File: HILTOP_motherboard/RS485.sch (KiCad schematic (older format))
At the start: 42 parts, among them U13 AM1S-0505SZ, U15 ISO3080, U16 ISO3080, U17 AM1S-0505SZ, U18 USB6B1, U19 USB6B1, U20 USB6B1, U21 USB6B1, U43 MAX3107, U44 MAX3107, Y8 3.6864MHz Crystal, Y9 3.6864MHz Crystal

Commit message: nearly finished placing all parts!
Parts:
- L5, L6: value 15uH -> 10uH; Devtank 112-007 -> 112-004
- U13, U17: value AM1S-0505SZ -> CME0505S3C; Devtank 131-002 -> 131-003
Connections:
- net +5V: now also C44.2, C78.2, U13.2 (+VIN), U17.2 (+VIN); no longer L5.1, L6.1
- net +5V_ISO3: now also L5.2; no longer U13.4 (+VOUT)
- net +5V_ISO4: now also L6.2; no longer U17.4 (+VOUT)
- new net: L5.1, U13.4 (+VOUT)
- new net: L6.1, U17.4 (+VOUT)
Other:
- moved on the sheet: C43, C44, C45, C46, C76, C78, L5, L6, U13, U17

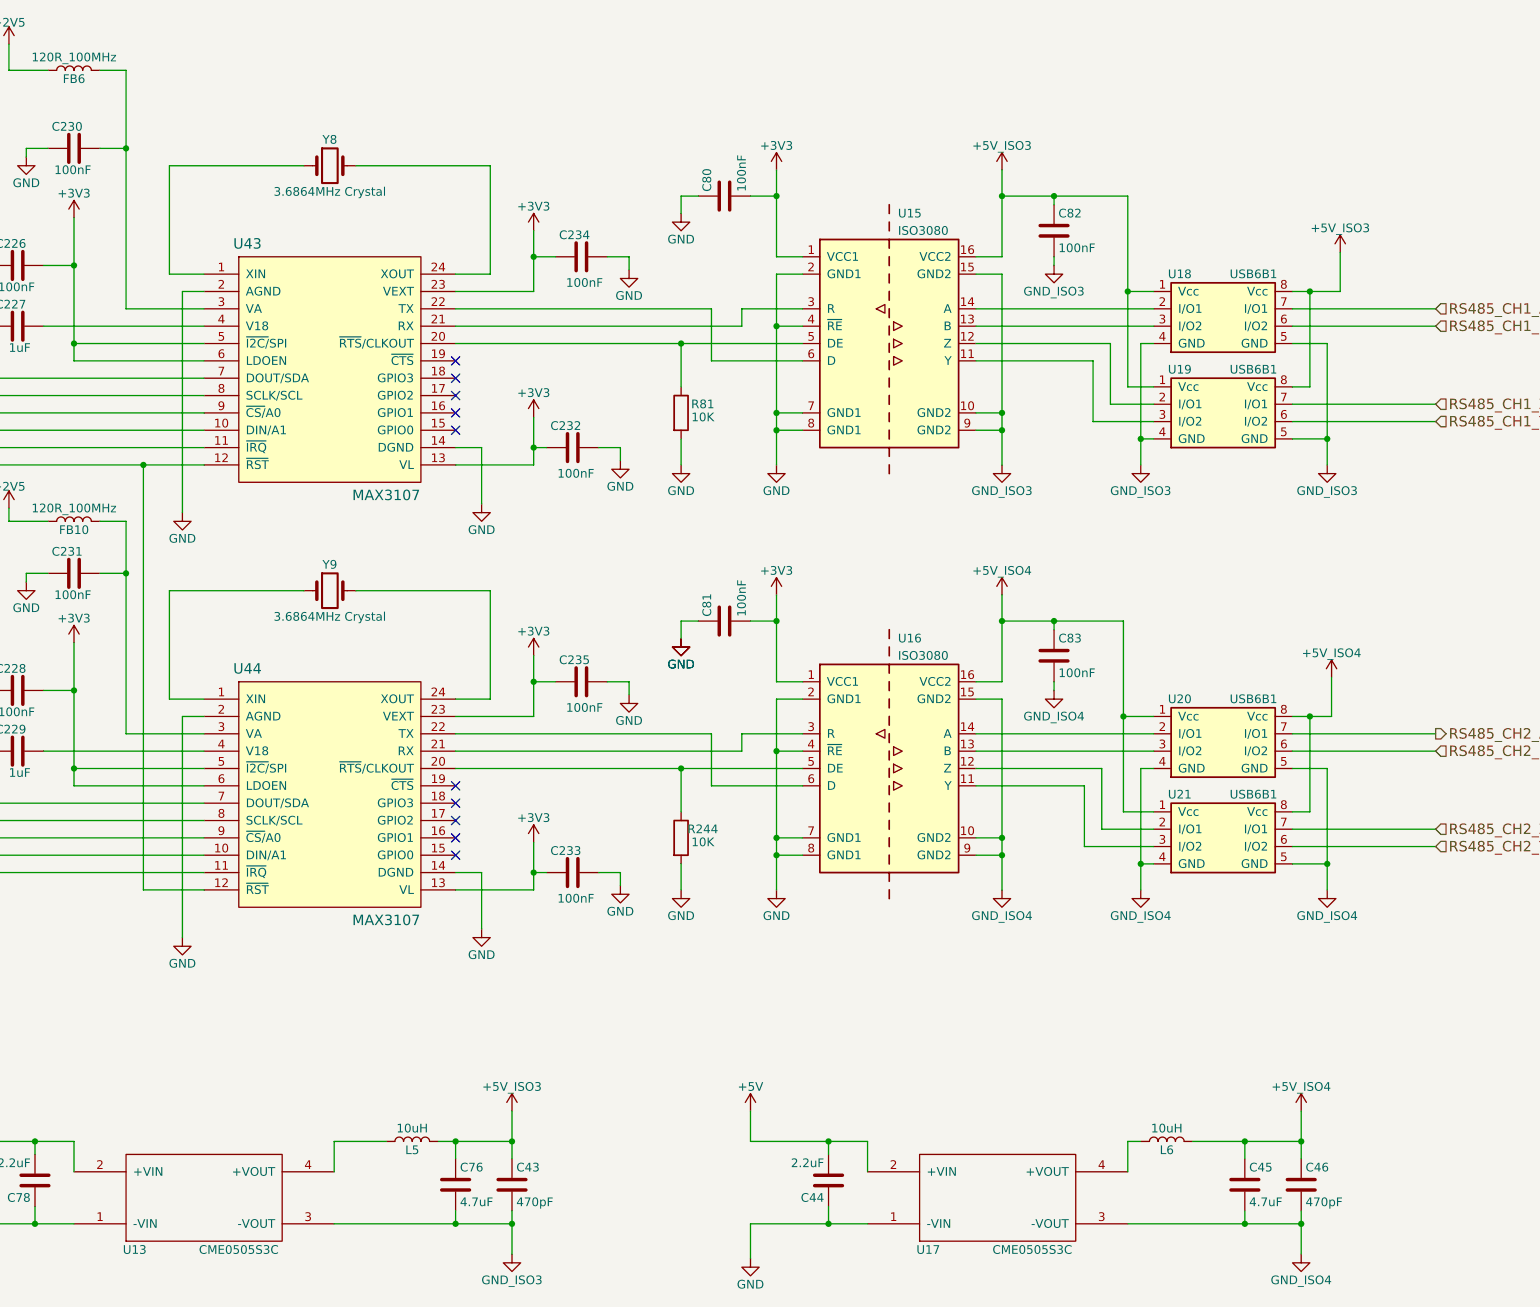
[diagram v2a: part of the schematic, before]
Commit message: DRC checks complete, all errors and warnings cleared. BOM created and parts rationalised.
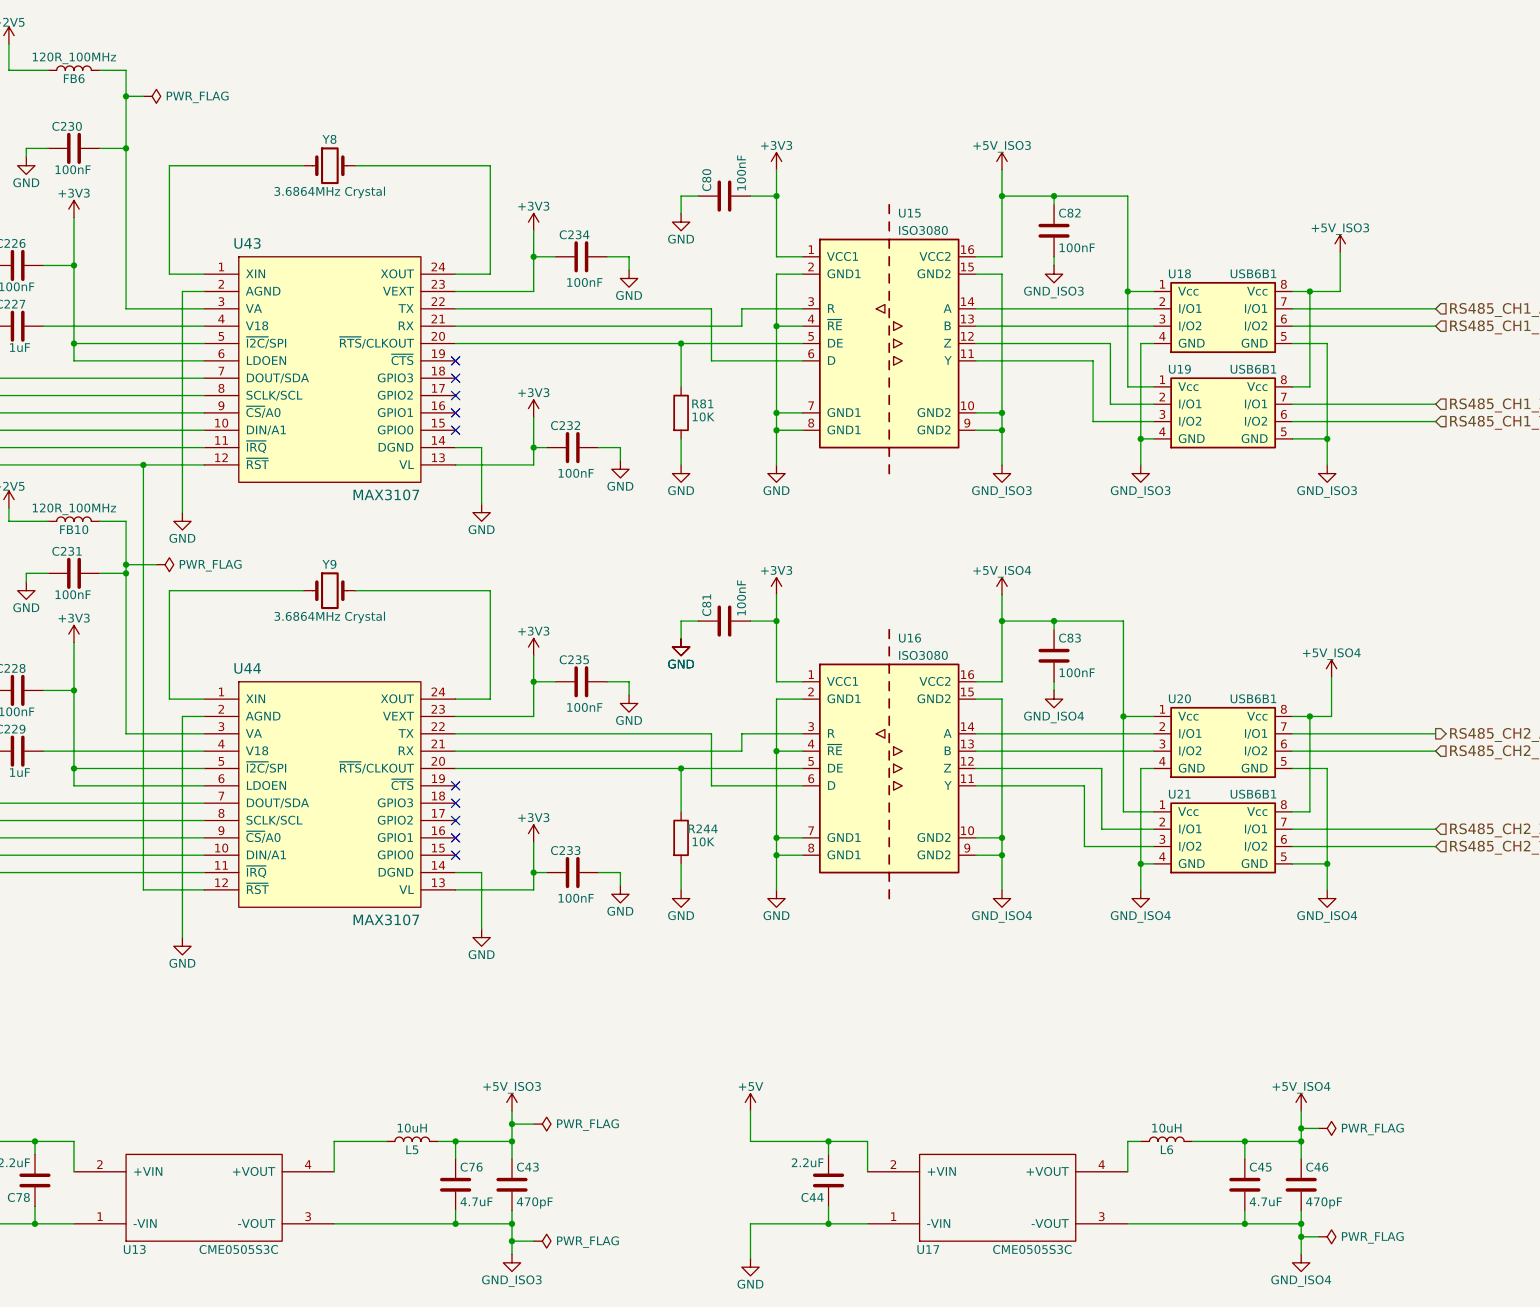
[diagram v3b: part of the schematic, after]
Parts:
- C227, C229: Devtank 105-012 -> 105-014
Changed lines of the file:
@@
 $EndComp
 Wire Wire Line
-	6050 7350 6050 7525
+	6050 7350 6050 7425
 Wire Wire Line
 	5725 7625 5725 7525
@@
 $EndComp
 Wire Wire Line
-	10600 7350 10600 7525
+	10600 7350 10600 7450
 Wire Wire Line
 	10275 7625 10275 7525
@@
 	5725 7525 6050 7525
 Wire Wire Line
-	6050 8000 6050 8175
+	6050 8000 6050 8100
 Wire Wire Line
 	6050 7525 6050 7625
@@
 	10275 7525 10600 7525
 Wire Wire Line
-	10600 8000 10600 8175
+	10600 8000 10600 8075
 Wire Wire Line
 	10600 7525 10600 7625
@@
 F 2 "Capacitor_SMD:C_0603_1608Metric" H 3238 2675 50  0001 C CNN
 F 3 "" H 3200 2825 50  0000 C CNN
-F 4 "105-012" H 3200 2825 60  0001 C CNN "Devtank"
+F 4 "105-014" H 3200 2825 60  0001 C CNN "Devtank"
 	1    3200 2825
 	0    -1   -1   0
@@
 	3675 1350 3825 1350
 Wire Wire Line
-	3825 1350 3825 1800
+	3825 1350 3825 1500
 Wire Wire Line
 	3375 1350 3150 1350
@@
 F 2 "Capacitor_SMD:C_0603_1608Metric" H 3238 5125 50  0001 C CNN
 F 3 "" H 3200 5275 50  0000 C CNN
-F 4 "105-012" H 3200 5275 60  0001 C CNN "Devtank"
+F 4 "105-014" H 3200 5275 60  0001 C CNN "Devtank"
 	1    3200 5275
 	0    -1   -1   0
@@
 	3675 3950 3825 3950
 Wire Wire Line
-	3825 3950 3825 4250
+	3825 3950 3825 4200
 Wire Wire Line
 	3375 3950 3150 3950
@@
 Wire Wire Line
 	9600 8000 10275 8000
+$Comp
+L power:PWR_FLAG #FLG0117
+U 1 1 5CF0D991
+P 6175 7425
+F 0 "#FLG0117" H 6175 7500 50  0001 C CNN
+F 1 "PWR_FLAG" V 6175 7553 50  0000 L CNN
+F 2 "" H 6175 7425 50  0001 C CNN
+F 3 "" H 6175 7425 50  0001 C CNN
+	1    6175 7425
+	0    1    1    0
+$EndComp
+$Comp
+L power:PWR_FLAG #FLG0118
+U 1 1 5CF0DBA5
+P 6175 8100
+F 0 "#FLG0118" H 6175 8175 50  0001 C CNN
+F 1 "PWR_FLAG" V 6175 8228 50  0000 L CNN
+F 2 "" H 6175 8100 50  0001 C CNN
+F 3 "" H 6175 8100 50  0001 C CNN
+	1    6175 8100
+	0    1    1    0
+$EndComp
+Wire Wire Line
+	6175 8100 6050 8100
+Connection ~ 6050 8100
+Wire Wire Line
+	6050 8100 6050 8175
+Wire Wire Line
+	6175 7425 6050 7425
+Connection ~ 6050 7425
+Wire Wire Line
+	6050 7425 6050 7525
+$Comp
+L power:PWR_FLAG #FLG0119
+U 1 1 5CF42CCF
+P 10700 7450
+F 0 "#FLG0119" H 10700 7525 50  0001 C CNN
+F 1 "PWR_FLAG" V 10700 7578 50  0000 L CNN
+F 2 "" H 10700 7450 50  0001 C CNN
+F 3 "" H 10700 7450 50  0001 C CNN
+	1    10700 7450
+	0    1    1    0
+$EndComp
+$Comp
+L power:PWR_FLAG #FLG0120
+U 1 1 5CF42D2E
+P 10700 8075
+F 0 "#FLG0120" H 10700 8150 50  0001 C CNN
+F 1 "PWR_FLAG" V 10700 8203 50  0000 L CNN
+F 2 "" H 10700 8075 50  0001 C CNN
+F 3 "" H 10700 8075 50  0001 C CNN
+	1    10700 8075
+	0    1    1    0
+$EndComp
+Wire Wire Line
+	10700 8075 10600 8075
+Connection ~ 10600 8075
+Wire Wire Line
+	10600 8075 10600 8175
+Wire Wire Line
+	10700 7450 10600 7450
+Connection ~ 10600 7450
+Wire Wire Line
+	10600 7450 10600 7525
+$Comp
+L power:PWR_FLAG #FLG0127
+U 1 1 5DF62965
+P 3925 1500
+F 0 "#FLG0127" H 3925 1575 50  0001 C CNN
+F 1 "PWR_FLAG" V 3925 1628 50  0000 L CNN
+F 2 "" H 3925 1500 50  0001 C CNN
+F 3 "" H 3925 1500 50  0001 C CNN
+	1    3925 1500
+	0    1    1    0
+$EndComp
+Wire Wire Line
+	3925 1500 3825 1500
+Connection ~ 3825 1500
+Wire Wire Line
+	3825 1500 3825 1800
+$Comp
+L power:PWR_FLAG #FLG0128
+U 1 1 5DF7E225
+P 4000 4200
+F 0 "#FLG0128" H 4000 4275 50  0001 C CNN
+F 1 "PWR_FLAG" V 4000 4328 50  0000 L CNN
+F 2 "" H 4000 4200 50  0001 C CNN
+F 3 "" H 4000 4200 50  0001 C CNN
+	1    4000 4200
+	0    1    1    0
+$EndComp
+Wire Wire Line
+	4000 4200 3825 4200
+Connection ~ 3825 4200
+Wire Wire Line
+	3825 4200 3825 4250
 $EndSCHEMATC

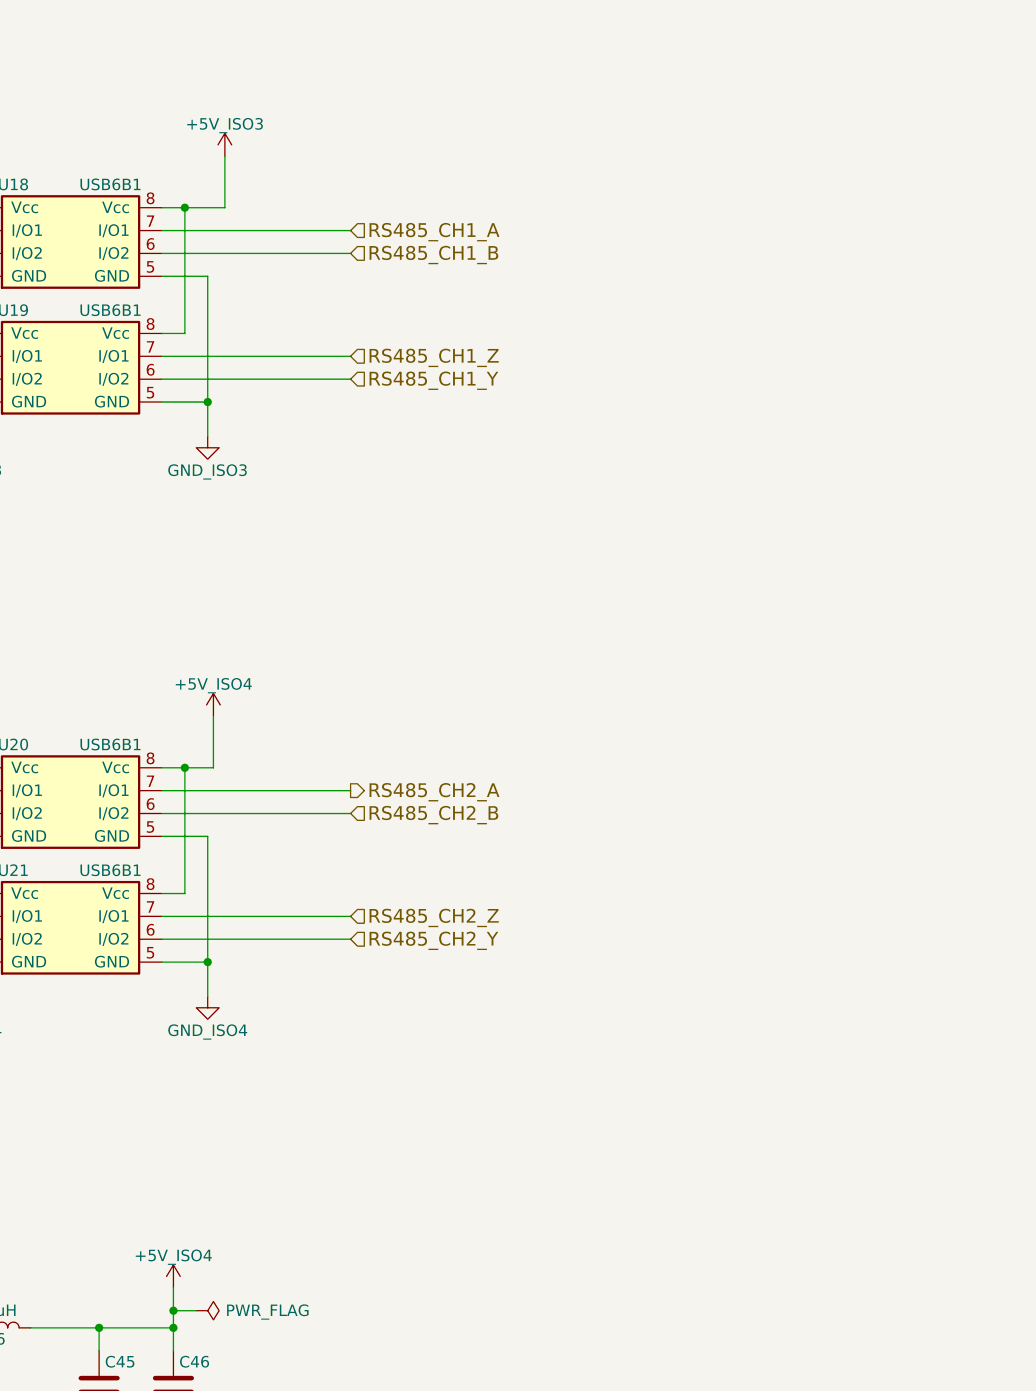
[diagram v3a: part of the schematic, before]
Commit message: finished new tracking for RS485 signals and general house keeping
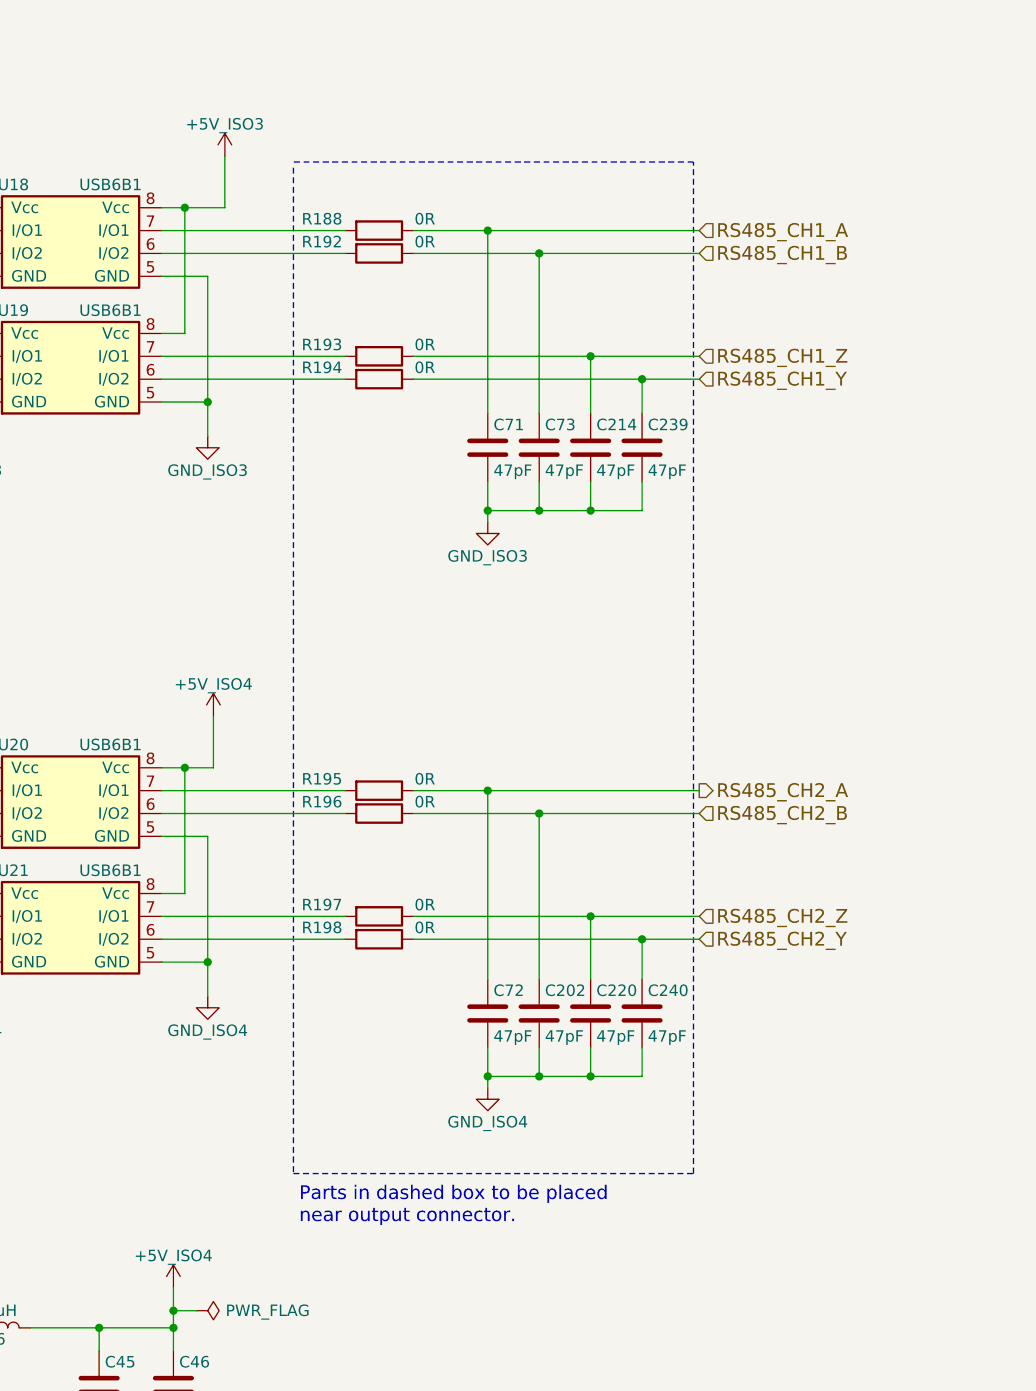
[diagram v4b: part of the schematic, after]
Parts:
- added C202, C214, C220, C239, C240, C71, C72, C73: 47pF, Capacitor_SMD:C_0603_1608Metric, symbol device:C
- added R188, R192, R193, R194, R195, R196, R197, R198: 0R, Resistor_SMD:R_0603_1608Metric, symbol device:R
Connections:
- net GND_ISO3: now also C214.2, C239.2, C71.2, C73.2
- net GND_ISO4: now also C202.2, C220.2, C240.2, C72.2
- net RS485_CH1_A: now also C71.1, R188.1; no longer U18.7 (I/O1)
- net RS485_CH1_B: now also C73.1, R192.1; no longer U18.6 (I/O2)
- net RS485_CH1_Y: now also C239.1, R194.1; no longer U19.6 (I/O2)
- net RS485_CH1_Z: now also C214.1, R193.1; no longer U19.7 (I/O1)
- net RS485_CH2_A: now also C72.1, R195.1; no longer U20.7 (I/O1)
- net RS485_CH2_B: now also C202.1, R196.1; no longer U20.6 (I/O2)
- net RS485_CH2_Y: now also C240.1, R198.1; no longer U21.6 (I/O2)
- net RS485_CH2_Z: now also C220.1, R197.1; no longer U21.7 (I/O1)
- new net: R192.2, U18.6 (I/O2)
- new net: R188.2, U18.7 (I/O1)
- new net: R194.2, U19.6 (I/O2)
- new net: R193.2, U19.7 (I/O1)
- new net: R196.2, U20.6 (I/O2)
- new net: R195.2, U20.7 (I/O1)
- new net: R198.2, U21.6 (I/O2)
- new net: R197.2, U21.7 (I/O1)
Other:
- note added: "Parts in dashed box to be placed\nnear output connector."

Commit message: Rev B
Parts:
- C202, C214, C220, C239, C240, C71, C72, C73: Devtank 106-001 -> 106-011
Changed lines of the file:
@@
 F 2 "Capacitor_SMD:C_0603_1608Metric" H 12013 6000 50  0001 C CNN
 F 3 "" H 11975 6150 50  0000 C CNN
-F 4 "106-001" H 11975 6150 60  0001 C CNN "Devtank"
+F 4 "106-011" H 11975 6150 60  0001 C CNN "Devtank"
 	1    11975 6150
 	1    0    0    -1
@@
 F 2 "Capacitor_SMD:C_0603_1608Metric" H 12238 6000 50  0001 C CNN
 F 3 "" H 12200 6150 50  0000 C CNN
-F 4 "106-001" H 12200 6150 60  0001 C CNN "Devtank"
+F 4 "106-011" H 12200 6150 60  0001 C CNN "Devtank"
 	1    12200 6150
 	1    0    0    -1
@@
 F 2 "Capacitor_SMD:C_0603_1608Metric" H 12463 6000 50  0001 C CNN
 F 3 "" H 12425 6150 50  0000 C CNN
-F 4 "106-001" H 12425 6150 60  0001 C CNN "Devtank"
+F 4 "106-011" H 12425 6150 60  0001 C CNN "Devtank"
 	1    12425 6150
 	1    0    0    -1
@@
 F 2 "Capacitor_SMD:C_0603_1608Metric" H 12688 6000 50  0001 C CNN
 F 3 "" H 12650 6150 50  0000 C CNN
-F 4 "106-001" H 12650 6150 60  0001 C CNN "Devtank"
+F 4 "106-011" H 12650 6150 60  0001 C CNN "Devtank"
 	1    12650 6150
 	1    0    0    -1
@@
 F 2 "Capacitor_SMD:C_0603_1608Metric" H 12013 3525 50  0001 C CNN
 F 3 "" H 11975 3675 50  0000 C CNN
-F 4 "106-001" H 11975 3675 60  0001 C CNN "Devtank"
+F 4 "106-011" H 11975 3675 60  0001 C CNN "Devtank"
 	1    11975 3675
 	1    0    0    -1
@@
 F 2 "Capacitor_SMD:C_0603_1608Metric" H 12238 3525 50  0001 C CNN
 F 3 "" H 12200 3675 50  0000 C CNN
-F 4 "106-001" H 12200 3675 60  0001 C CNN "Devtank"
+F 4 "106-011" H 12200 3675 60  0001 C CNN "Devtank"
 	1    12200 3675
 	1    0    0    -1
@@
 F 2 "Capacitor_SMD:C_0603_1608Metric" H 12463 3525 50  0001 C CNN
 F 3 "" H 12425 3675 50  0000 C CNN
-F 4 "106-001" H 12425 3675 60  0001 C CNN "Devtank"
+F 4 "106-011" H 12425 3675 60  0001 C CNN "Devtank"
 	1    12425 3675
 	1    0    0    -1
@@
 F 2 "Capacitor_SMD:C_0603_1608Metric" H 12688 3525 50  0001 C CNN
 F 3 "" H 12650 3675 50  0000 C CNN
-F 4 "106-001" H 12650 3675 60  0001 C CNN "Devtank"
+F 4 "106-011" H 12650 3675 60  0001 C CNN "Devtank"
 	1    12650 3675
 	1    0    0    -1
